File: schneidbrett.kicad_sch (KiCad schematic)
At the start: 7 parts

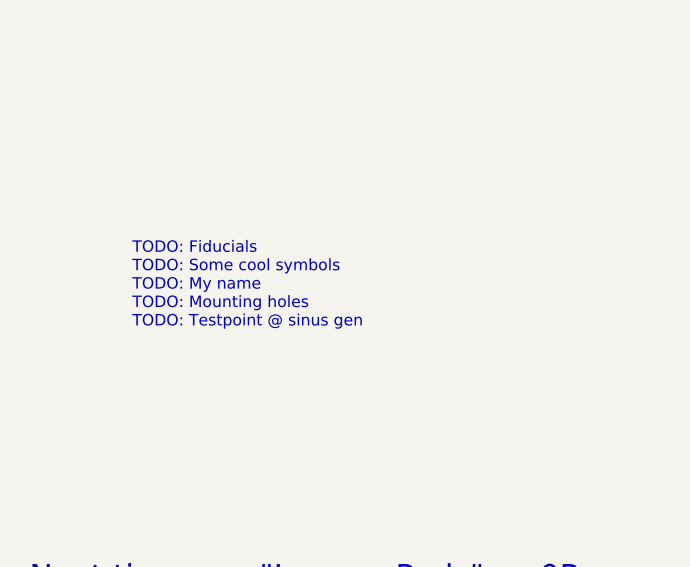
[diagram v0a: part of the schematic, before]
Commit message: Added ESD, updated Footprints, BOM, etc.
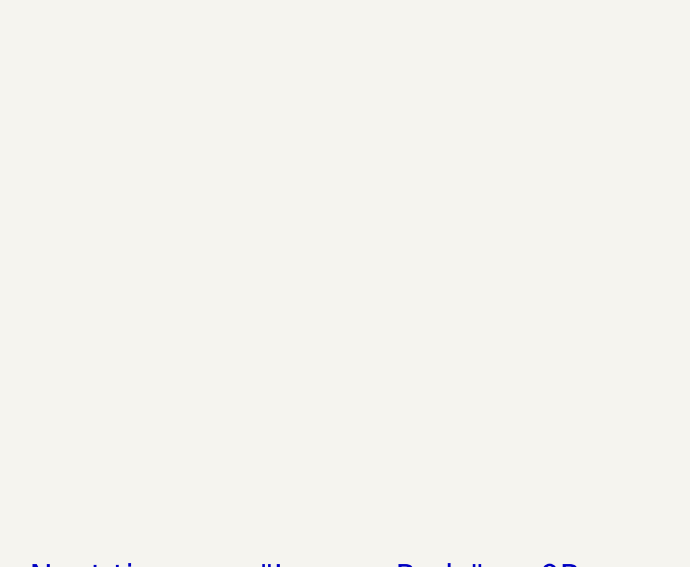
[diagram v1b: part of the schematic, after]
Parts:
- FID1, FID2, FID3, H1, H2, H3, H4: now left out of the parts list
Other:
- note removed: "TODO: Fiducials TODO: Some cool symbols TODO: My name TODO: Mounting holes TODO: Testpoint @ sinus gen"
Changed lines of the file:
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@@
     (effects (font (size 1.27 1.27)) (justify left top))
-  )
-  (text "TODO: Fiducials\nTODO: Some cool symbols\nTODO: My name\nTODO: Mounting holes\nTODO: Testpoint @ sinus gen\n"
-    (at 25.4 96.52 0)
-    (effects (font (size 1.27 1.27)) (justify left bottom))
   )
   (text "Meta" (at 229.87 80.01 0)
@@
   )
   (symbol (lib_id "Mechanical:MountingHole_Pad") (at 257.81 107.95 270) (unit 1)
-    (in_bom yes) (on_board yes) (dnp no) (fields_autoplaced)
+    (in_bom no) (on_board yes) (dnp no) (fields_autoplaced)
     (property "Reference" "H3" (at 261.62 106.68 90)
       (effects (font (size 1.27 1.27)) (justify left))
@@
   )
   (symbol (lib_id "Mechanical:MountingHole_Pad") (at 257.81 82.55 270) (unit 1)
-    (in_bom yes) (on_board yes) (dnp no) (fields_autoplaced)
+    (in_bom no) (on_board yes) (dnp no) (fields_autoplaced)
     (property "Reference" "H1" (at 261.62 81.28 90)
       (effects (font (size 1.27 1.27)) (justify left))
@@
   )
   (symbol (lib_id "Mechanical:Fiducial") (at 234.95 107.95 0) (unit 1)
-    (in_bom yes) (on_board yes) (dnp no) (fields_autoplaced)
+    (in_bom no) (on_board yes) (dnp no) (fields_autoplaced)
     (property "Reference" "FID3" (at 237.49 106.68 0)
       (effects (font (size 1.27 1.27)) (justify left))
@@
   )
   (symbol (lib_id "Mechanical:Fiducial") (at 234.95 95.25 0) (unit 1)
-    (in_bom yes) (on_board yes) (dnp no) (fields_autoplaced)
+    (in_bom no) (on_board yes) (dnp no) (fields_autoplaced)
     (property "Reference" "FID2" (at 237.49 93.98 0)
       (effects (font (size 1.27 1.27)) (justify left))
@@
   )
   (symbol (lib_id "Mechanical:Fiducial") (at 234.95 82.55 0) (unit 1)
-    (in_bom yes) (on_board yes) (dnp no) (fields_autoplaced)
+    (in_bom no) (on_board yes) (dnp no) (fields_autoplaced)
     (property "Reference" "FID1" (at 237.49 81.28 0)
       (effects (font (size 1.27 1.27)) (justify left))
@@
   )
   (symbol (lib_id "Mechanical:MountingHole_Pad") (at 257.81 95.25 270) (unit 1)
-    (in_bom yes) (on_board yes) (dnp no) (fields_autoplaced)
+    (in_bom no) (on_board yes) (dnp no) (fields_autoplaced)
     (property "Reference" "H2" (at 261.62 93.98 90)
       (effects (font (size 1.27 1.27)) (justify left))
@@
   )
   (symbol (lib_id "Mechanical:MountingHole_Pad") (at 257.81 120.65 270) (unit 1)
-    (in_bom yes) (on_board yes) (dnp no) (fields_autoplaced)
+    (in_bom no) (on_board yes) (dnp no) (fields_autoplaced)
     (property "Reference" "H4" (at 261.62 119.38 90)
       (effects (font (size 1.27 1.27)) (justify left))
